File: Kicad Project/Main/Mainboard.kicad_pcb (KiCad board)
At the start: 2 copper layers, 83.8 x 63.5 mm, 102 parts, among them J1 ICSP, J2 USB, P1 CONN_01X02, Q1 FDC638, Q2 FZT788B, Q3 FZT788B, U1 LTC4412, U10 FT230X, U11 LM75BDP, U12 HIH6130, U2 ATmega328P, U3 LTC6800, U4 LTC6800, U5 ADS1015, U6 bq2057CTS, U7 bq2057CTS, U8 SM72238, U9 LMR61428, X1 32kHz

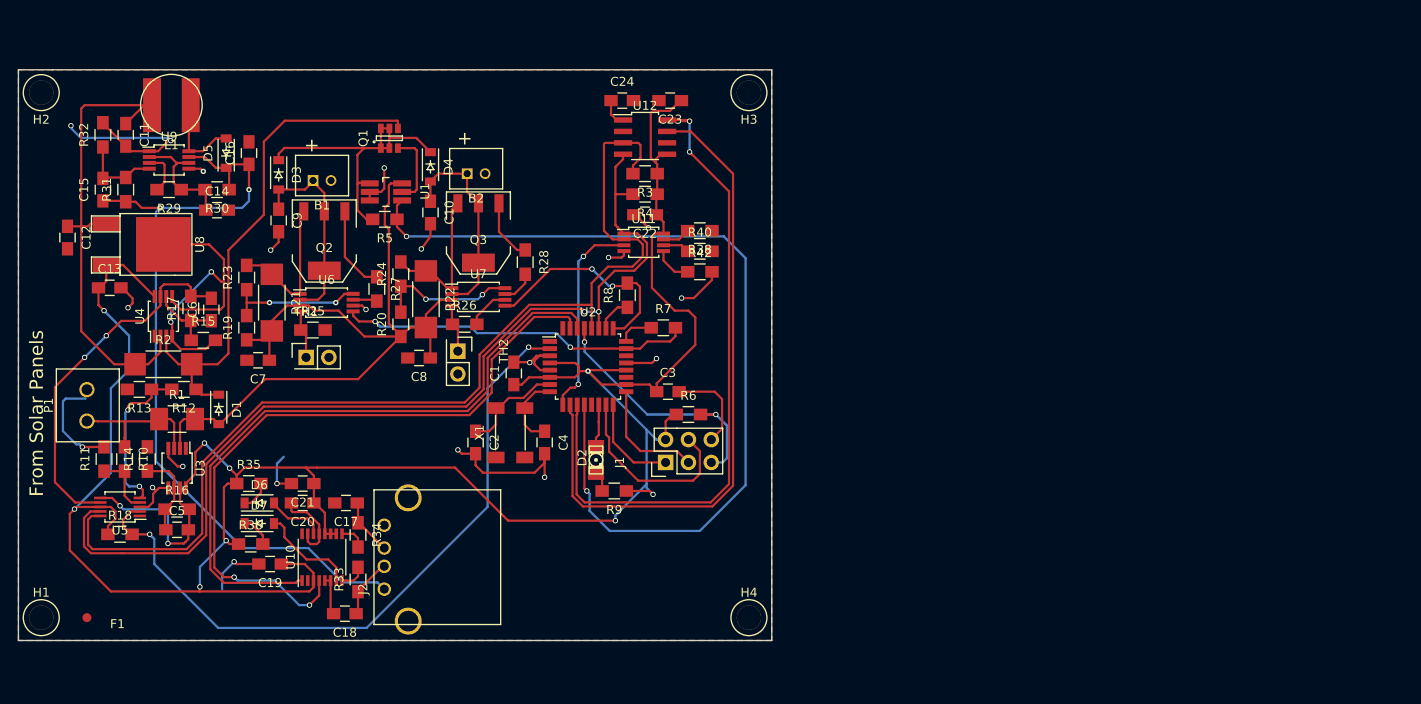
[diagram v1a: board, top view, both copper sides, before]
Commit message: Created third revison of the mainboard Created manufacturing files for the mainboard Deleated the MPPT board project
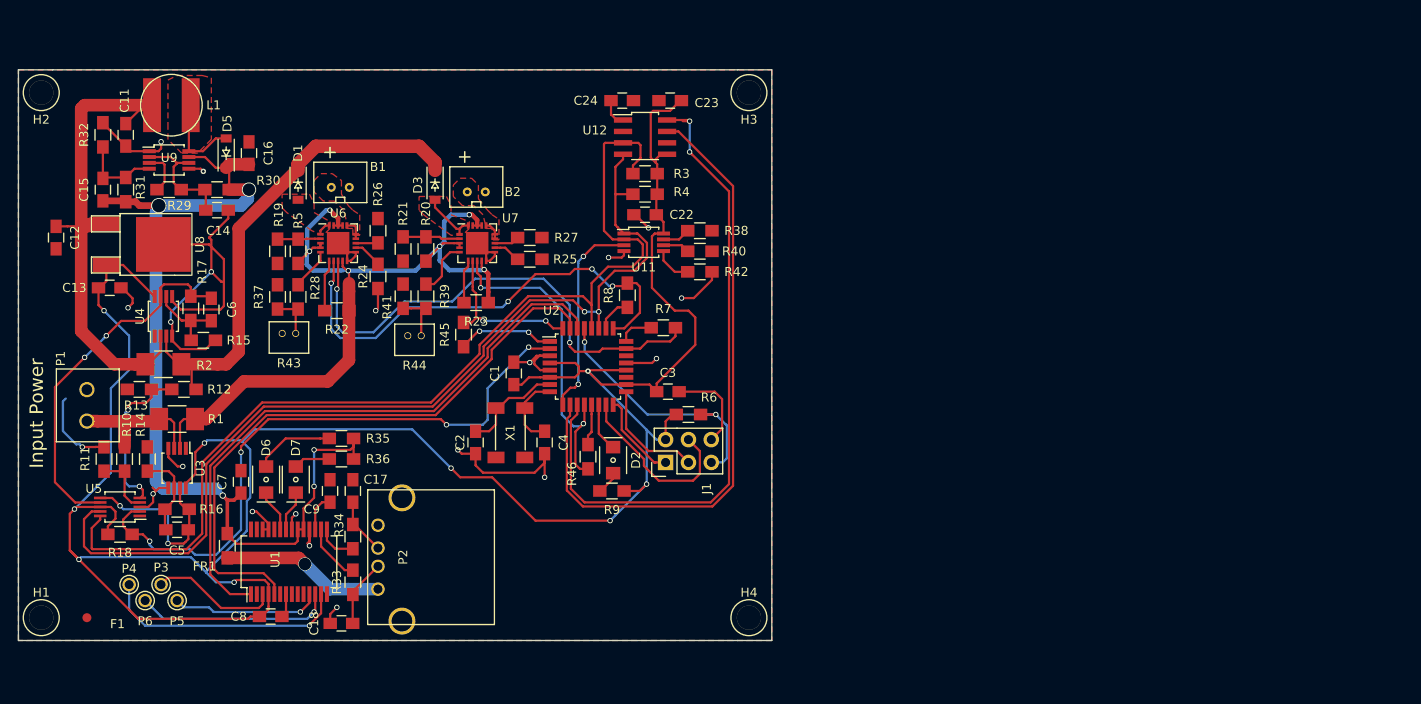
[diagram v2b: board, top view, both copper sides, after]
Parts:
- removed ?: Symbol_OSHW-Logo_SilkScreen, Symbols:Symbol_OSHW-Logo_SilkScreen
- removed C10: 0.1uF, Capacitors_SMD:C_0805_HandSoldering
- removed C19, C20: 100nF, Capacitors_SMD:C_0805_HandSoldering
- removed C21: 4.7uF, Capacitors_SMD:C_0805_HandSoldering
- removed D4: 1N5819, Diodes_SMD:SOD-123
- removed the G*** at (112.6, 107.3)
- removed J2: USB, Connect:USB_A
- removed Q1: FDC638, RFCX:FDC-SOT-23-6
- removed Q2, Q3: FZT788B, SMD_Packages:SOT-223
- removed TH1, TH2: NTC, Pin_Headers:Pin_Header_Straight_2x01
- removed U10: FT230X, Housings_SSOP:SSOP-16_3.9x4.9mm_Pitch0.635mm
- added FR1: Ferrite, Resistors_SMD:R_0805_HandSoldering, F.Cu at (124.2, 106.9)
- added P2: USB_A, Connect:USB_A, F.Cu at (141.0, 111.8)
- added P3: CONN_01X01, Connect:1pin, F.Cu at (116.8, 111.3)
- added P4: CONN_01X01, Connect:1pin, F.Cu at (113.3, 111.3)
- added P5: CONN_01X01, Connect:1pin, F.Cu at (118.6, 113.0)
- added P6: CONN_01X01, Connect:1pin, F.Cu at (115.1, 113.0)
- added R37: 10k, Resistors_SMD:R_0805_HandSoldering, F.Cu at (129.8, 79.2)
- added R39: 1k, Resistors_SMD:R_0805_HandSoldering, F.Cu at (146.3, 79.2)
- added R41: 10k, Resistors_SMD:R_0805_HandSoldering, F.Cu at (143.8, 79.2)
- added R43: NTC, RFCx:JST-1.5mm, F.Cu at (131.1, 83.3)
- added R44: NTC, RFCx:JST-1.5mm, F.Cu at (145.0, 83.6)
- added R45: 1k, Resistors_SMD:R_0805_HandSoldering, F.Cu at (150.5, 83.4)
- added R46: 1k, Resistors_SMD:R_0805_HandSoldering, F.Cu at (164.3, 97.0)
- added REF**: Symbol_OSHW-Logo_SilkScreen, Symbols:Symbol_OSHW-Logo_SilkScreen, B.Cu at (175.0, 104.4)
- B1, B2: value Li-ion(2Cell) -> Li-ion-2cell-conn; footprint RFCX:JST_BAT -> RFCx:JST-2mm
- C24: value 0.1 -> 0.1uF
- D2: footprint LEDs:LED-1206 -> RFCx:LED-1208
- D5: value Diode-Shottky -> 1N5819
- D6: footprint Diodes_SMD:SOD-123 -> RFCx:LED-1208
- D7: value LED -> YLW; footprint Diodes_SMD:SOD-123 -> RFCx:LED-1208
- R1: value Res -> 0.51, 1W
- R17: value Res -> 2550
- R19: value 10k -> 100k
- R2: value 0.5,1W -> 0.51 ,1W; footprint Resistors_SMD:R_2010_HandSoldering -> Resistors_SMD:R_1210_HandSoldering
- R20: value 10k -> 270k
- R21: value 0.2, 1W -> 100k; footprint Resistors_SMD:R_2010_HandSoldering -> Resistors_SMD:R_0805_HandSoldering
- R22: value 0.2, 1W -> 1k; footprint Resistors_SMD:R_2010_HandSoldering -> Resistors_SMD:R_0805_HandSoldering
- R23: value 5k -> 1k
- R24: value 5k -> Res
- R25, R26: value 49.9k -> Res
- R27: value 1k -> Res
- R3: value 10k -> 4.7k
- R35, R36: value 730 -> 270
- R5: value 470k -> 270k
- U1: value LTC4412 -> FT232R; footprint Housings_SOT-23_SOT-143_TSOT-6:TSOT-6-MK06A_Handsoldering -> Housings_SSOP:SSOP-28_5.3x10.2mm_Pitch0.65mm
- U6, U7: value bq2057CTS -> MCP73871; footprint SSOP:TSSOP-8_4.4x3mm_Pitch0.65mm -> Housings_DFN_QFN:QFN-20-1EP_4x4mm_Pitch0.5mm
- moved U1 42.5 mm to (131.1, 108.7), turned to 90 degrees
- moved C8 33.2 mm to (129.0, 114.8), turned to 0 degrees
- moved C9 30.6 mm to (135.6, 100.8), turned to 90 degrees
- moved D1 26.5 mm to (132.1, 66.8)
- moved R23 25.7 mm to (151.9, 79.9), turned to 180 degrees
- moved R28 25.6 mm to (132.1, 79.2)
- moved R25 25.4 mm to (157.9, 75.1)
- moved G*** 21.3 mm to (154.3, 107.1)
- moved R27 18.0 mm to (157.9, 72.6), turned to 0 degrees
- moved D3 17.4 mm to (147.3, 66.8)
- moved R21 15.8 mm to (143.8, 73.9)
- moved R26 14.2 mm to (141.0, 71.9), turned to 90 degrees
- moved R36 13.8 mm to (136.9, 97.3), turned to 180 degrees
- moved C7 13.7 mm to (125.7, 99.8), turned to 90 degrees
- moved R35 11.5 mm to (136.9, 95.0), turned to 180 degrees
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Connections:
- C7 pad 1: /ADC/Input-Current-L -> +5V
- C8 pad 1: /ADC/Input-Current-L -> +3V3
- C9 pad 1: Net-(B1-Pad1) -> Net-(C9-Pad1)
- D1 pad 1: /ADC/Output-Current-H -> /Battery Charging/Bat-Out
- D1 pad 2: /ADC/Input-Current-L -> Net-(D1-Pad2)
- D3 pad 1: /Battery Management/Battery-Vout -> /Battery Charging/Bat-Out
- D3 pad 2: Net-(B1-Pad1) -> Net-(D3-Pad2)
- R1 pad 2: /ADC/Input-Current-L -> /Battery Charging/Bat-In
- R12 pad 1: /ADC/Output-Current-H -> /Battery Charging/Bat-Out
- R19 pad 1: /ADC/Input-Current-L -> Net-(R19-Pad1)
- R19 pad 2: Net-(R19-Pad2) -> GND
- R2 pad 2: /ADC/Output-Current-H -> /Battery Charging/Bat-Out
- R20 pad 1: /ADC/Input-Current-L -> /Battery Charging/Bat-In
- R21 pad 1: Net-(Q2-Pad3) -> Net-(R20-Pad2)
- R21 pad 2: /ADC/Input-Current-L -> GND
- R22 pad 1: Net-(Q3-Pad3) -> /Battery Charging/Bat-In
- R22 pad 2: /ADC/Input-Current-L -> Net-(R22-Pad2)
- R23 pad 1: Net-(R19-Pad2) -> /Battery Charging/Bat-In
- R23 pad 2: Net-(Q2-Pad3) -> Net-(R23-Pad2)
- R24 pad 1: Net-(R20-Pad2) -> Net-(R24-Pad1)
- R24 pad 2: Net-(Q3-Pad3) -> GND
- R27 pad 1: Net-(Q2-Pad1) -> Net-(R27-Pad1)
- R27 pad 2: Net-(R27-Pad2) -> GND
- R28 pad 1: Net-(Q3-Pad1) -> Net-(R28-Pad1)
- R35 pad 1: +3V3 -> +5V
- R35 pad 2: Net-(D6-Pad1) -> Net-(D6-Pad2)
- R36 pad 1: +3V3 -> +5V
- R36 pad 2: Net-(D7-Pad1) -> Net-(D7-Pad2)
- R5 pad 1: /Microcontroller/PPM_STAT -> /Battery Charging/Bat-In
- R5 pad 2: /Battery Management/Battery-Vout -> Net-(R19-Pad1)
- R7 pad 2: /Microcontroller/AT-BAT1-STAT -> /Microcontroller/AT-BAT1-STAT1
- R8 pad 2: /Microcontroller/AT-BAT2-STAT -> /Microcontroller/AT-BAT1-STAT2
- R9 pad 2: Net-(D2-Pad1) -> Net-(D2-Pad2)
- U1 pad 1: /Battery Management/Battery-Vout -> /Microcontroller/AT-RXD
- U1 pad 2: GND -> (no net)
- U1 pad 3: GND -> Net-(P3-Pad1)
- U1 pad 4: /Microcontroller/PPM_STAT -> +3V3
- U1 pad 5: Net-(Q1-Pad2) -> /Microcontroller/AT-TXD
- U1 pad 6: /ADC/Input-Current-L -> (no net)
- U12 pad 7: Net-(U12-Pad7) -> (no net)
- U2 pad 12: /Microcontroller/PPM_STAT -> /Microcontroller/AT-BAT2-STAT1
- U2 pad 14: Net-(D2-Pad2) -> Net-(D2-Pad1)
- U2 pad 19: Net-(U2-Pad19) -> (no net)
- U2 pad 22: Net-(U2-Pad22) -> (no net)
- U2 pad 23: /Microcontroller/AT-BAT1-STAT -> /Microcontroller/AT-BAT1-STAT1
- U2 pad 25: /Microcontroller/AT-BAT2-STAT -> /Microcontroller/AT-BAT1-STAT2
- U2 pad 32: Net-(U2-Pad32) -> /Microcontroller/AT-BAT2-STAT2
- U3 pad 2: /ADC/Input-Current-L -> /Battery Charging/Bat-In
- U4 pad 3: /ADC/Output-Current-H -> /Battery Charging/Bat-Out
- U6 pad 1: Net-(Q2-Pad3) -> Net-(D1-Pad2)
- U6 pad 2: Net-(B1-Pad1) -> Net-(R19-Pad1)
- U6 pad 3: /ADC/Input-Current-L -> /Battery Charging/Bat-In
- U6 pad 4: Net-(R25-Pad1) -> /Battery Charging/Bat-In
- U6 pad 5: /Microcontroller/AT-BAT1-STAT -> Net-(R28-Pad1)
- U6 pad 6: GND -> Net-(R22-Pad2)
- U6 pad 7: Net-(R27-Pad2) -> /Microcontroller/AT-BAT1-STAT2
- U6 pad 8: Net-(R19-Pad2) -> /Microcontroller/AT-BAT1-STAT1
- U7 pad 1: Net-(Q3-Pad3) -> Net-(D3-Pad2)
- U7 pad 2: Net-(B2-Pad1) -> Net-(R20-Pad2)
- U7 pad 3: /ADC/Input-Current-L -> /Battery Charging/Bat-In
- U7 pad 4: Net-(R26-Pad1) -> /Battery Charging/Bat-In
- U7 pad 5: /Microcontroller/AT-BAT2-STAT -> Net-(R39-Pad1)
- U7 pad 6: GND -> Net-(R23-Pad2)
- U7 pad 7: Net-(R28-Pad2) -> /Microcontroller/AT-BAT2-STAT2
- U7 pad 8: Net-(R20-Pad2) -> /Microcontroller/AT-BAT2-STAT1
- X1 pad 2: Net-(X1-Pad2) -> (no net)
- X1 pad 3: Net-(X1-Pad3) -> (no net)
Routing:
- net /Microcontroller/PPM_STAT: track 101.1 -> 0.00 mm, vias 2 -> 0
- net /Battery Charging/Bat-In: track 0.00 -> 94.6 mm, vias 0 -> 6
- net /ADC/Input-Current-L: track 87.1 -> 0.00 mm
- net /ADC/Output-Current-H: track 57.4 -> 0.00 mm
- net /Microcontroller/AT-BAT1-STAT1: track 0.00 -> 55.5 mm, vias 0 -> 2
- net /Battery Charging/Bat-Out: track 0.00 -> 55.4 mm
- net /Microcontroller/AT-BAT1-STAT2: track 0.00 -> 53.3 mm, vias 0 -> 4
- net /Microcontroller/AT-BAT1-STAT: track 39.4 -> 0.00 mm, vias 2 -> 0
- net /Microcontroller/AT-BAT2-STAT1: track 0.00 -> 36.6 mm, vias 0 -> 2
- net /Battery Management/Battery-Vout: track 34.9 -> 0.00 mm
- net Net-(P4-Pad1): track 0.00 -> 27.6 mm, vias 0 -> 1
- net /Microcontroller/AT-BAT2-STAT: track 24.4 -> 0.00 mm, vias 2 -> 0
- net Net-(P6-Pad1): track 0.00 -> 22.0 mm, vias 0 -> 1
- net Net-(B2-Pad1): track 22.8 -> 2.10 mm
- net Net-(B1-Pad1): track 22.3 -> 2.35 mm
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- added copper zone on F.Cu, net Net-(B1-Pad1)
- added copper zone on F.Cu, net Net-(B2-Pad1)
- added copper zone on F.Cu, net Net-(D1-Pad2)
- added copper zone on F.Cu, net Net-(D3-Pad2)
- added copper zone on F.Cu, net Net-(D5-Pad2)
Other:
- net class PWR added: clearance 0.5, trace_width 1.4, via_dia 1.5, via_drill 1.4
- board text added: "Input Power"
- board text added: "Rainforest Connection Mainboard Rev C Jesse Millwood"
- board text removed: "From Solar Panels"
- board text removed: "In Conjuntion With"
- board text removed: "Main Sensor/Charging Board Rev: B Designed By: Jesse Millwood (GVSU) Joe Gibson (GVSU) June 2015"

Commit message: Revision 3 of Sentinal PCB major changes:  - This is one PCB now  - The MPPT circuitry has been taken off  - Libraries have been moved around  - The FTDI FT232R is being used  - A buck boost regulator is being used to charge the phone  - Readme was updated
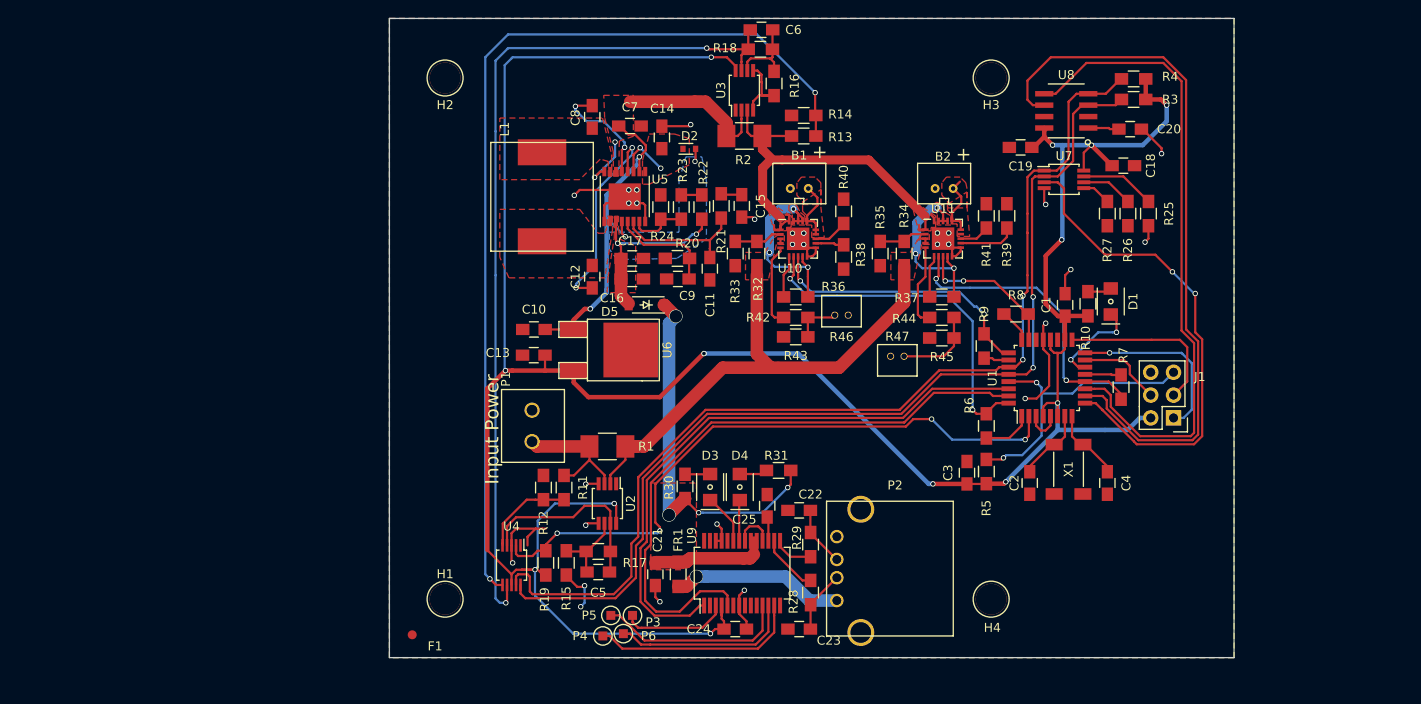
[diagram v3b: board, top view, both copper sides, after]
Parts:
- removed D6: GRN, RFCx:LED-1208
- removed D7: YLW, RFCx:LED-1208
- removed the G*** at (154.3, 107.1)
- removed U12: HIH6130, RFCX:HIH-SOIC-8
- added C10: 1uF, Capacitors_SMD:C_0805_HandSoldering, F.Cu at (158.3, 82.9)
- added C19: 0.22uF, Capacitors_SMD:C_0805_HandSoldering, F.Cu at (212.5, 62.6)
- added C20: 0.1uF, Capacitors_SMD:C_0805_HandSoldering, F.Cu at (224.7, 60.6)
- added C21: 0.1uF, Capacitors_SMD:C_0805_HandSoldering, F.Cu at (171.8, 110.1)
- added C25: 0.1uF, Capacitors_SMD:C_0805_HandSoldering, F.Cu at (184.3, 102.5)
- added D4: YLW, RFCx:LED-1208, F.Cu at (181.2, 100.4)
- added G***: LOGO, Graphics:rfcx, B.Cu at (217.9, 101.1)
- added R47: NTC, RFCx:JST-1.5mm, F.Cu at (198.8, 85.9)
- added U10: MCP73871, Housings_DFN_QFN:QFN-20-1EP_4x4mm_Pitch0.5mm, F.Cu at (187.7, 72.8)
- C11: value 22uF Tant -> 10p
- C12: value 1uF -> 68nF
- C14: value 1uF -> 4.7uF
- C15: value 39pF -> 4700pF
- C16: value 68uF Tant -> 22uF
- C17: value 47pF -> 22uF
- C18: value 47pF -> 0.1uF
- C22: value 0.1uF -> 47pF
- C23: value 0.22uF -> 47pF
- C7: value 0.1uF -> 10uF
- C8: value 0.1uF -> 68nF
- C9: value 0.1uF -> 10nF
- D1: value 1N5819 -> LED; footprint Diodes_SMD:SOD-123 -> RFCx:LED-1208
- D2: value LED -> PMEG2010AEB; footprint RFCx:LED-1208 -> Diodes_SMD:SOD-523
- D3: value 1N5819 -> GRN; footprint Diodes_SMD:SOD-123 -> RFCx:LED-1208
- D5: value 1N5819 -> RB161M-20
- L1: value 6.8uH -> 68uH; footprint RFCX:Ind_6x6 -> RFCx:Ind-Wurth-12_1x11_4
- R10: value 1540 -> 730
- R11, R13: value 2100 -> 1540
- R12: value 1540 -> 2100
- R14: value 200k -> 2100
- R16: value 2550 -> 200k
- R18: value 10k -> 2550
- R19: value 100k -> 10k
- R2: value 0.51 ,1W -> 0.51, 1W
- R20: value 270k -> 21k
- R21: value 100k -> 27.4k
- R22: value 1k -> 49.9
- R23: value 1k -> 2M
- R24: value Res -> 499k
- R25, R26, R27: value Res -> 10k
- R28: value 1k -> 27
- R29: value 200k -> 27
- R30: value 49.9 -> 270
- R31: value 150k -> 270
- R32: value 49.9k -> 270k
- R33: value 27 -> 100k
- R34: value 27 -> 270k
- R35: value 270 -> 100k
- R36: value 270 -> 1k
- R37, R42, R6: value 10k -> 1k
- R38: value 10k -> 100k
- R39: value 1k -> 100k
- R4: value 10k -> 4.7k
- R40, R41: value 10k -> 1.14k
- R43: value NTC -> 10k; footprint RFCx:JST-1.5mm -> Resistors_SMD:R_0805_HandSoldering
- R44: value NTC -> 1k; footprint RFCx:JST-1.5mm -> Resistors_SMD:R_0805_HandSoldering
- R45: value 1k -> 10k
- R46: value 1k -> NTC; footprint Resistors_SMD:R_0805_HandSoldering -> RFCx:JST-1.5mm
- R5: value 270k -> 10k
- R9: value 730 -> 1k
- U1: value FT232R -> ATmega328P; footprint Housings_SSOP:SSOP-28_5.3x10.2mm_Pitch0.65mm -> Housings_QFP:TQFP-32_7x7mm_Pitch0.8mm
- U11: value LM75BDP -> MCP73871; footprint SSOP:MSOP-8_3x3mm_Pitch0.65mm -> Housings_DFN_QFN:QFN-20-1EP_4x4mm_Pitch0.5mm
- U2: value ATmega328P -> LTC6800; footprint Housings_QFP:TQFP-32_7x7mm_Pitch0.8mm -> Housings_SSOP:MSOP-8_3x3mm_Pitch0.65mm
- U3: footprint SSOP:MSOP-8_3x3mm_Pitch0.65mm -> Housings_SSOP:MSOP-8_3x3mm_Pitch0.65mm
- U4: value LTC6800 -> ADS1015; footprint SSOP:MSOP-8_3x3mm_Pitch0.65mm -> Housings_SSOP:MSOP-10_3x3mm_Pitch0.5mm
- U5: value ADS1015 -> LTC3114-1; footprint Housings_SSOP:MSOP-10_3x3mm_Pitch0.5mm -> Housings_SSOP:TSSOP-16-1EP_4.4x5mm_Pitch0.65mm
- U6: value MCP73871 -> SM72238; footprint Housings_DFN_QFN:QFN-20-1EP_4x4mm_Pitch0.5mm -> TO_SOT_Packages_SMD:TO-252-2Lead
- U7: value MCP73871 -> LM75BDP; footprint Housings_DFN_QFN:QFN-20-1EP_4x4mm_Pitch0.5mm -> Housings_SSOP:MSOP-8_3x3mm_Pitch0.65mm
- U8: value SM72238 -> HIH6130; footprint SMD_Packages:DPAK-2 -> RFCx:HIH-SOIC-8
- U9: value LMR61428 -> FT232R; footprint SSOP:MSOP-8_3x3mm_Pitch0.65mm -> Housings_SSOP:SSOP-28_5.3x10.2mm_Pitch0.65mm
- moved R10 108.6 mm to (220.0, 80.0), turned to 90 degrees
- moved U8 107.8 mm to (217.6, 58.5), turned to 180 degrees
- moved C18 100.8 mm to (223.9, 64.6), turned to 0 degrees
- moved D1 91.3 mm to (222.5, 79.8), turned to 90 degrees
- moved R18 89.4 mm to (183.5, 51.7), turned to 180 degrees
- moved U1 86.8 mm to (215.4, 88.3)
- moved R26 83.5 mm to (224.4, 70.0), turned to 270 degrees
- moved R14 82.4 mm to (188.3, 59.1), turned to 180 degrees
- moved R16 81.6 mm to (185.0, 55.5), turned to 270 degrees
- moved R29 81.6 mm to (189.1, 106.8), turned to 270 degrees
- moved R5 80.4 mm to (208.7, 98.7)
- moved R13 79.1 mm to (188.3, 61.3), turned to 0 degrees
- moved R31 79.1 mm to (185.5, 98.6), turned to 180 degrees
- moved U9 78.6 mm to (181.5, 110.0), turned to 90 degrees
- moved U3 75.8 mm to (181.7, 56.3), turned to 90 degrees
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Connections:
- B1 pad 1: Net-(B1-Pad1) -> GND
- B1 pad 2: GND -> Net-(B1-Pad2)
- B2 pad 1: Net-(B2-Pad1) -> GND
- B2 pad 2: GND -> Net-(B2-Pad2)
- C11 pad 1: /ADC/Output-Current-L -> Net-(C11-Pad1)
- C12 pad 1: /ADC/Output-Current-L -> Net-(C12-Pad1)
- C12 pad 2: GND -> Net-(C12-Pad2)
- C15 pad 1: +5V -> Net-(C15-Pad1)
- C15 pad 2: /+3.3V and +5V Regulation/LM_FB -> GND
- C16 pad 1: +5V -> Net-(C16-Pad1)
- C17 pad 1: Net-(C17-Pad1) -> Net-(C16-Pad1)
- C18 pad 1: Net-(C18-Pad1) -> +3V3
- C22 pad 1: +3V3 -> Net-(C22-Pad1)
- C23 pad 1: +3V3 -> Net-(C23-Pad1)
- C24 pad 1: Net-(C24-Pad1) -> +3V3
- C7 pad 1: +5V -> /ADC/Output-Current-L
- C8 pad 1: +3V3 -> Net-(C8-Pad1)
- C8 pad 2: GND -> Net-(C8-Pad2)
- D1 pad 1: /Battery Charging/Bat-Out -> Net-(D1-Pad1)
- D2 pad 1: Net-(D2-Pad1) -> Net-(C14-Pad1)
- D2 pad 2: Net-(D2-Pad2) -> Net-(C16-Pad1)
- D3 pad 1: /Battery Charging/Bat-Out -> Net-(D3-Pad1)
- D5 pad 2: Net-(D5-Pad2) -> Net-(C16-Pad1)
- L1 pad 1: /ADC/Output-Current-L -> Net-(C8-Pad1)
- L1 pad 2: Net-(D5-Pad2) -> Net-(C12-Pad1)
- P2 pad 2: Net-(C18-Pad1) -> Net-(C23-Pad1)
- P2 pad 3: Net-(C17-Pad1) -> Net-(C22-Pad1)
- R10 pad 1: /ADC/Input-Current-H -> +3V3
- R10 pad 2: Net-(R10-Pad2) -> Net-(D1-Pad2)
- R11 pad 1: Net-(R10-Pad2) -> /ADC/Input-Current-H
- R11 pad 2: GND -> Net-(R11-Pad2)
- R12 pad 1: /Battery Charging/Bat-Out -> Net-(R11-Pad2)
- R12 pad 2: Net-(R12-Pad2) -> GND
- R13 pad 1: Net-(R12-Pad2) -> /Battery Charging/Bat-Out
- R13 pad 2: GND -> Net-(R13-Pad2)
- R14 pad 1: Net-(C5-Pad1) -> Net-(R13-Pad2)
- R15 pad 1: Net-(C6-Pad1) -> Net-(C5-Pad1)
- R16 pad 1: Net-(C5-Pad1) -> Net-(C6-Pad1)
- R16 pad 2: Net-(C5-Pad2) -> GND
- R17 pad 1: Net-(C6-Pad1) -> Net-(C5-Pad1)
- R17 pad 2: Net-(C6-Pad2) -> Net-(C5-Pad2)
- R18 pad 1: +3V3 -> Net-(C6-Pad1)
- R18 pad 2: /Microcontroller/AT-Alert -> Net-(C6-Pad2)
- R19 pad 1: Net-(R19-Pad1) -> +3V3
- R19 pad 2: GND -> /Microcontroller/AT-Alert
- R20 pad 1: /Battery Charging/Bat-In -> Net-(C9-Pad1)
- R20 pad 2: Net-(R20-Pad2) -> GND
- R21 pad 1: Net-(R20-Pad2) -> Net-(C11-Pad1)
- R21 pad 2: GND -> Net-(C15-Pad1)
- R22 pad 1: /Battery Charging/Bat-In -> Net-(C16-Pad1)
- R23 pad 1: /Battery Charging/Bat-In -> Net-(R22-Pad2)
- R24 pad 1: Net-(R24-Pad1) -> Net-(R23-Pad2)
- R25 pad 1: Net-(R25-Pad1) -> GND
- R25 pad 2: GND -> Net-(R25-Pad2)
- R28 pad 1: Net-(R28-Pad1) -> Net-(C23-Pad1)
- R29 pad 1: Net-(C14-Pad1) -> Net-(C22-Pad1)
- R30 pad 2: Net-(C14-Pad1) -> Net-(D3-Pad2)
- R31 pad 2: /+3.3V and +5V Regulation/LM_FB -> Net-(D4-Pad2)
- R32 pad 1: /+3.3V and +5V Regulation/LM_FB -> /Battery Charging/Bat-In
- R32 pad 2: GND -> Net-(R32-Pad2)
- R33 pad 1: Net-(C18-Pad1) -> Net-(R32-Pad2)
- R33 pad 2: Net-(R33-Pad2) -> GND
- R34 pad 1: Net-(C17-Pad1) -> /Battery Charging/Bat-In
- R35 pad 1: +5V -> Net-(R34-Pad2)
- R35 pad 2: Net-(D6-Pad2) -> GND
- R36 pad 1: +5V -> /Battery Charging/Bat-In
- R37 pad 1: Net-(R28-Pad2) -> /Battery Charging/Bat-In
- R37 pad 2: GND -> Net-(R37-Pad2)
- R38 pad 1: GND -> Net-(R38-Pad1)
- R38 pad 2: Net-(R38-Pad2) -> GND
- R39 pad 2: Net-(R39-Pad2) -> GND
- R41 pad 1: Net-(R39-Pad2) -> Net-(R41-Pad1)
- R42 pad 2: GND -> Net-(R42-Pad2)
- R43 pad 1: Net-(R28-Pad2) -> Net-(R42-Pad2)
- R44 pad 1: Net-(R39-Pad2) -> Net-(R44-Pad1)
- R44 pad 2: GND -> Net-(R44-Pad2)
- R45 pad 1: Net-(R45-Pad1) -> Net-(R44-Pad2)
- R45 pad 2: /Microcontroller/AT-BAT2-STAT2 -> GND
- R46 pad 1: Net-(R46-Pad1) -> Net-(R42-Pad2)
- R46 pad 2: /Microcontroller/AT-BAT2-STAT1 -> GND
- R5 pad 1: /Battery Charging/Bat-In -> +3V3
- R5 pad 2: Net-(R19-Pad1) -> Net-(J1-Pad5)
- R6 pad 1: +3V3 -> Net-(R6-Pad1)
- R6 pad 2: Net-(J1-Pad5) -> /Microcontroller/AT-BAT1-STAT2
- R7 pad 2: /Microcontroller/AT-BAT1-STAT1 -> /Microcontroller/AT-BAT2-STAT2
- R8 pad 2: /Microcontroller/AT-BAT1-STAT2 -> /Microcontroller/AT-BAT2-STAT1
- R9 pad 1: +3V3 -> Net-(R9-Pad1)
- R9 pad 2: Net-(D2-Pad2) -> /Microcontroller/AT-BAT1-STAT1
- U1 pad 1: /Microcontroller/AT-RXD -> Net-(R6-Pad1)
- U1 pad 10: (no net) -> /Environment Sensors/ENV_AL_L
- U1 pad 11: Net-(P5-Pad1) -> /Environment Sensors/ENV_AL_H
- U1 pad 12: Net-(P6-Pad1) -> /Microcontroller/AT-BAT2-STAT2
- U1 pad 13: Net-(P4-Pad1) -> Net-(R7-Pad1)
- U1 pad 14: (no net) -> Net-(D1-Pad1)
- U1 pad 15: Net-(R34-Pad2) -> Net-(J1-Pad4)
- U1 pad 16: Net-(R33-Pad2) -> Net-(J1-Pad1)
- U1 pad 17: Net-(C9-Pad1) -> Net-(J1-Pad3)
- U1 pad 18: GND -> +3V3
- U1 pad 19: +5V -> (no net)
- U1 pad 2: (no net) -> /Microcontroller/AT-Alert
- U1 pad 20: +5V -> +3V3
- U1 pad 22: Net-(D7-Pad1) -> (no net)
- U1 pad 23: Net-(D6-Pad1) -> /Microcontroller/AT-BAT2-STAT1
- U1 pad 24: (no net) -> Net-(R8-Pad1)
- U1 pad 25: GND -> /Microcontroller/AT-BAT1-STAT1
- U1 pad 26: GND -> Net-(R9-Pad1)
- U1 pad 27: (no net) -> /Microcontroller/AT-SDA
- U1 pad 28: (no net) -> /Microcontroller/AT-SCL
- U1 pad 3: Net-(P3-Pad1) -> GND
- U1 pad 5: /Microcontroller/AT-TXD -> GND
- U1 pad 6: (no net) -> +3V3
- U1 pad 7: GND -> Net-(C2-Pad1)
- U1 pad 8: (no net) -> Net-(C4-Pad1)
- U1 pad 9: (no net) -> /Environment Sensors/ENV_OS
- U11 pad 1: /Microcontroller/AT-SDA -> /Battery Charging/Bat-Out
- U11 pad 2: /Microcontroller/AT-SCL -> Net-(R34-Pad2)
- U11 pad 3: /Environment Sensors/ENV_OS -> /Battery Charging/Bat-In
- U11 pad 4: GND -> /Battery Charging/Bat-In
- U11 pad 5: Net-(R42-Pad1) -> Net-(R44-Pad1)
- U11 pad 6: Net-(R40-Pad1) -> Net-(R37-Pad2)
- U11 pad 7: Net-(R38-Pad2) -> /Microcontroller/AT-BAT2-STAT2
- U11 pad 8: +3V3 -> /Microcontroller/AT-BAT2-STAT1
- U2 pad 1: Net-(R45-Pad1) -> (no net)
- U2 pad 2: /Microcontroller/AT-Alert -> /Battery Charging/Bat-In
- U2 pad 3: GND -> /ADC/Input-Current-H
- U2 pad 4: +3V3 -> GND
- U2 pad 6: +3V3 -> Net-(C5-Pad1)
- U2 pad 7: Net-(C2-Pad1) -> Net-(C5-Pad2)
- U2 pad 8: Net-(C4-Pad1) -> +3V3
- U3 pad 2: /Battery Charging/Bat-In -> /ADC/Output-Current-L
- U3 pad 3: /ADC/Input-Current-H -> /Battery Charging/Bat-Out
- U3 pad 6: Net-(C5-Pad1) -> Net-(C6-Pad1)
- U3 pad 7: Net-(C5-Pad2) -> Net-(C6-Pad2)
- U4 pad 2: /ADC/Output-Current-L -> /Microcontroller/AT-Alert
- U4 pad 3: /Battery Charging/Bat-Out -> GND
- U4 pad 4: GND -> Net-(C5-Pad2)
- U4 pad 5: GND -> Net-(R11-Pad2)
- U4 pad 6: Net-(C6-Pad1) -> Net-(R13-Pad2)
- U5 pad 1: (no net) -> GND
- U5 pad 10: /Microcontroller/AT-SCL -> /ADC/Output-Current-L
- U5 pad 2: /Microcontroller/AT-Alert -> Net-(C12-Pad1)
- U5 pad 3: GND -> Net-(C16-Pad1)
- U5 pad 4: Net-(R10-Pad2) -> /ADC/Output-Current-L
- U5 pad 5: Net-(R12-Pad2) -> Net-(C9-Pad1)
- U5 pad 6: Net-(C5-Pad2) -> Net-(C11-Pad1)
- U5 pad 7: Net-(C6-Pad2) -> Net-(R23-Pad2)
- U5 pad 8: +3V3 -> GND
- U5 pad 9: /Microcontroller/AT-SDA -> Net-(C14-Pad1)
- U6 pad 1: Net-(D1-Pad2) -> /ADC/Output-Current-L
- U6 pad 2: Net-(R19-Pad1) -> GND
- U6 pad 3: /Battery Charging/Bat-In -> +3V3
- U7 pad 1: Net-(D3-Pad2) -> /Microcontroller/AT-SDA
- U7 pad 2: Net-(R20-Pad2) -> /Microcontroller/AT-SCL
- U7 pad 3: /Battery Charging/Bat-In -> /Environment Sensors/ENV_OS
- U7 pad 4: /Battery Charging/Bat-In -> GND
- U7 pad 5: Net-(R39-Pad1) -> Net-(R27-Pad1)
- U7 pad 6: Net-(R23-Pad2) -> Net-(R26-Pad1)
- U7 pad 7: /Microcontroller/AT-BAT2-STAT2 -> Net-(R25-Pad2)
- U7 pad 8: /Microcontroller/AT-BAT2-STAT1 -> +3V3
- U8 pad 1: /ADC/Output-Current-L -> Net-(C20-Pad1)
- U8 pad 3: +3V3 -> /Microcontroller/AT-SCL
- U9 pad 1: GND -> /Microcontroller/AT-RXD
- U9 pad 2: Net-(C14-Pad1) -> (no net)
- U9 pad 3: Net-(R29-Pad2) -> Net-(P3-Pad1)
- U9 pad 4: /+3.3V and +5V Regulation/LM_FB -> +3V3
- U9 pad 5: GND -> /Microcontroller/AT-TXD
- U9 pad 6: Net-(C14-Pad1) -> (no net)
- U9 pad 7: +5V -> GND
- U9 pad 8: Net-(D5-Pad2) -> (no net)
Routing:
- net Net-(R13-Pad2): track 0.00 -> 105.2 mm, vias 0 -> 2
- net Net-(C6-Pad2): track 41.1 -> 97.0 mm
- net GND: track 152.3 -> 102.9 mm, vias 20 -> 29
- net +5V: track 102.5 -> 56.9 mm, vias 5 -> 4
- net /Environment Sensors/ENV_OS: track 22.8 -> 55.1 mm
- net /Microcontroller/AT-BAT1-STAT1: track 55.5 -> 30.7 mm
- net +3V3: track 275.6 -> 299.7 mm, vias 9 -> 13
- net Net-(C12-Pad2): track 0.00 -> 22.9 mm, vias 0 -> 2
- net Net-(C16-Pad1): track 0.00 -> 22.4 mm, vias 0 -> 3
- net /Microcontroller/AT-BAT2-STAT1: track 36.6 -> 16.5 mm
- net Net-(R12-Pad2): track 18.1 -> 0.00 mm, vias 2 -> 0
- net /Microcontroller/AT-BAT2-STAT2: track 18.2 -> 33.4 mm
- net Net-(C11-Pad1): track 0.00 -> 14.8 mm
- net /Microcontroller/AT-BAT1-STAT2: track 53.3 -> 39.5 mm, vias 4 -> 2
- net Net-(C8-Pad2): track 0.00 -> 12.7 mm, vias 0 -> 2
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- added copper zone on F.Cu, net +5V
- added copper zone on F.Cu, net /ADC/Output-Current-L
- added copper zone on F.Cu, net /Battery Charging/Bat-In
- added copper zone on F.Cu, net /Battery Charging/Bat-Out
- added copper zone on F.Cu, net Net-(B1-Pad2)
- added copper zone on F.Cu, net Net-(B2-Pad2)
- added copper zone on F.Cu, net Net-(C12-Pad1)
- added copper zone on F.Cu, net Net-(C14-Pad1)
- added copper zone on B.Cu, net Net-(C16-Pad1)
- added copper zone on F.Cu, net Net-(C8-Pad1)
- removed copper zone on F.Cu, net Net-(B1-Pad1)
- removed copper zone on F.Cu, net Net-(B2-Pad1)
- removed copper zone on F.Cu, net Net-(D1-Pad2)
- removed copper zone on F.Cu, net Net-(D3-Pad2)
- removed copper zone on F.Cu, net Net-(D5-Pad2)
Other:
- board size 83.8 x 63.5 mm -> 94 x 71.1 mm
- net class PWR-S added: clearance 0.2, trace_width 0.5, via_dia 0.6, via_drill 0.4
- board text added: "Rainforest Connection Sentinel Rev 3.1 (Nov. 2015) Jesse Millwood"
- board text removed: "Rainforest Connection Mainboard Rev C Jesse Millwood"

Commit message: Rev 3.1  - Added microphone filter schematic and board  - Added new silkscreen identifiers  - Added Reset button for microcontroller  - Fixed Address pin on ADS1015, pulled it up  - Created new Fabrication files
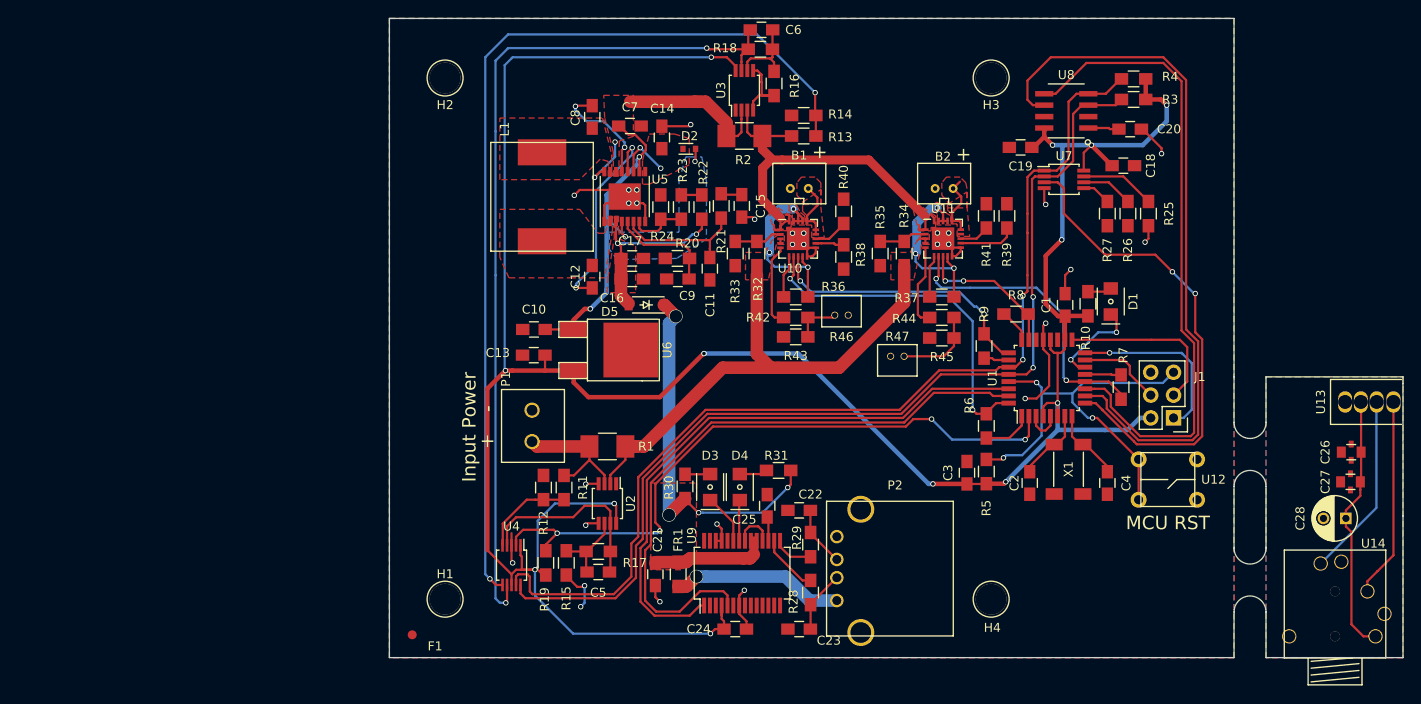
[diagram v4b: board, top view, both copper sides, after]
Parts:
- removed P3, P4, P5, P6: CONN_01X01, Connect:1pin
- added C26: Cap-X2Y, RFCx:C_0805_X2Y, F.Cu at (249.3, 96.5)
- added C27: Cap-X2Y, RFCx:C_0805_X2Y, F.Cu at (249.2, 99.8)
- added C28: DNP, Capacitors_ThroughHole:C_Radial_D5_L6_P2.5, F.Cu at (248.7, 103.9)
- added U12: Button_SPST_4, RFCx:SPST_4, F.Cu at (228.9, 99.6)
- added U13: 3.5mm-Male-TH, RFCx:Audio_3.5mm_Male_TH, F.Cu at (251.2, 90.9)
- added U14: 3.5mm-Female-TH, RFCx:Audio_3.5mm_Feale_TH, F.Cu at (247.5, 119.4)
- B1, B2: value Li-ion-2cell-conn -> Li-ion-2Cell-Conn
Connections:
- U4 pad 1: (no net) -> +3V3
- U9 pad 11: Net-(P5-Pad1) -> (no net)
- U9 pad 12: Net-(P6-Pad1) -> (no net)
- U9 pad 13: Net-(P4-Pad1) -> (no net)
- U9 pad 3: Net-(P3-Pad1) -> (no net)
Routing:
- net Net-(C26-Pad1): track 0.00 -> 28.9 mm
- net Net-(P4-Pad1): track 23.4 -> 0.00 mm
- net Net-(U13-Pad1): track 0.00 -> 22.3 mm
- net Net-(P5-Pad1): track 21.3 -> 0.00 mm
- net Net-(U13-Pad2): track 0.00 -> 20.5 mm
- net Net-(P6-Pad1): track 20.2 -> 0.00 mm
- net Net-(J1-Pad5): track 32.2 -> 47.7 mm, vias 2 -> 3
- net Net-(P3-Pad1): track 11.9 -> 0.00 mm
- net GND: track 102.9 -> 96.6 mm
- net +3V3: track 299.7 -> 302.5 mm
- net /Microcontroller/AT-Alert: track 71.9 -> 73.3 mm
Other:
- board size 94 x 71.1 mm -> 112.8 x 71.1 mm
- board text added: "-"
- board text added: "MCU RST"
